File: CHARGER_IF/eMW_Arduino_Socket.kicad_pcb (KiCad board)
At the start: 2 copper layers, 18 x 33 mm, 2 parts, among them J4 CONN_02X10, U2 Arduino-Socket

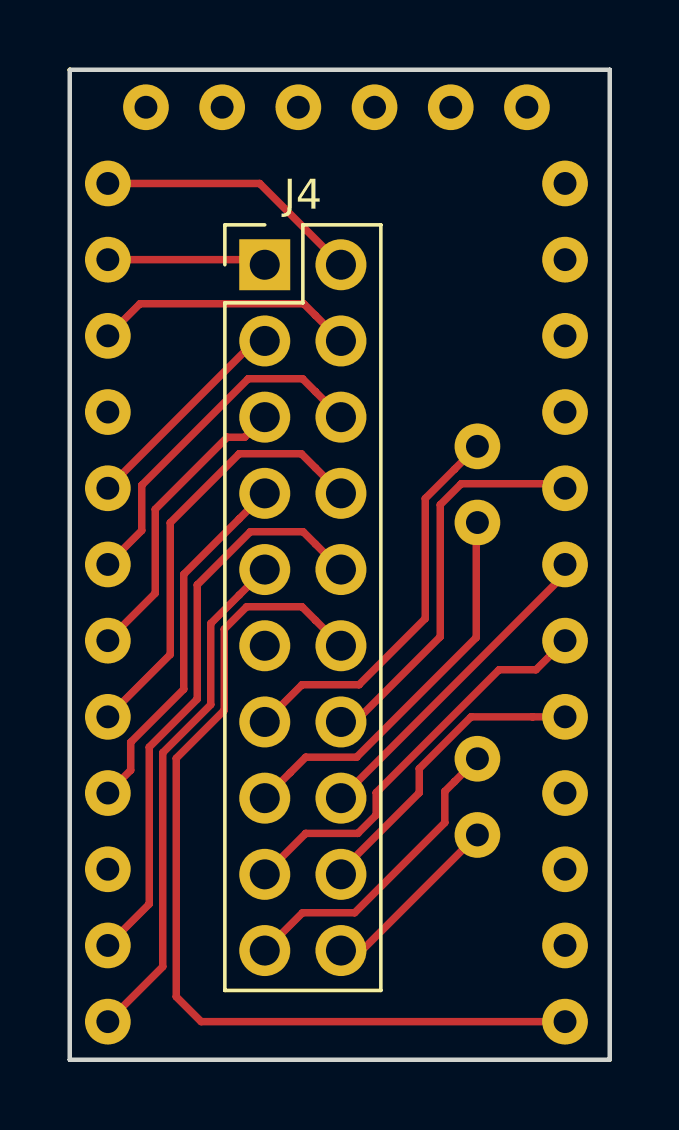
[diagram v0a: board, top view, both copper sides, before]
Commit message: updated to osh park design rules
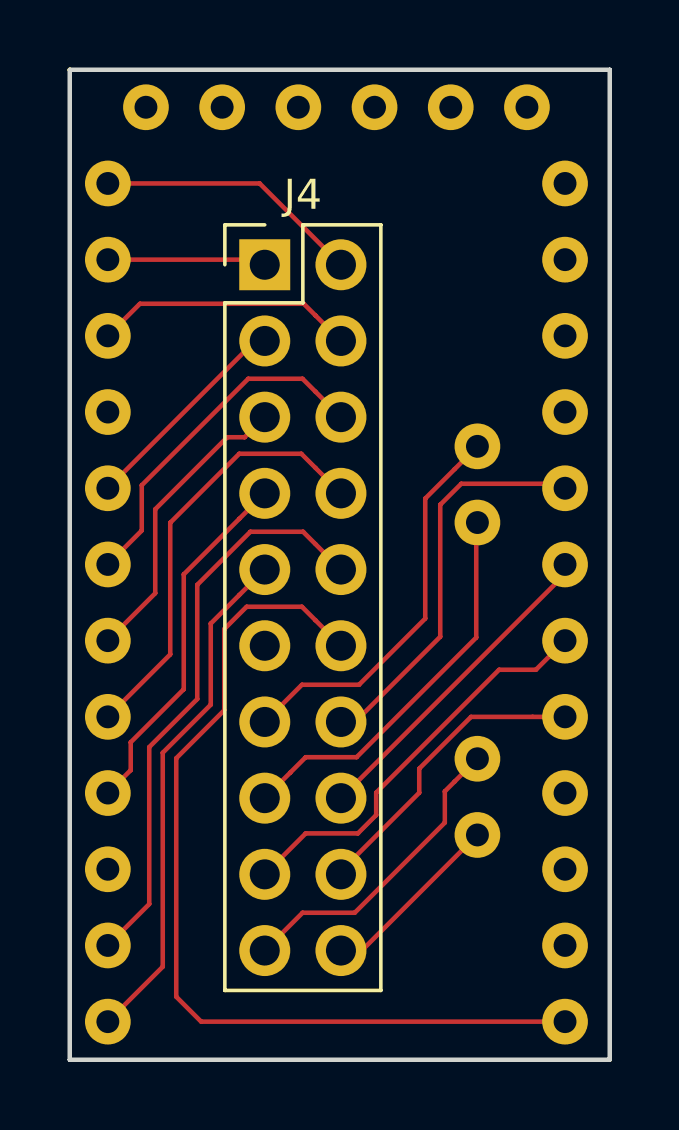
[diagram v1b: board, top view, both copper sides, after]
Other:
- net class Default: clearance 0.2 -> 0.1524; trace_width 0.25 -> 0.1524; via_dia 0.6 -> 0.6858; via_drill 0.4 -> 0.3302
- rule trace_clearance: 0.2 -> 0.1524
- rule trace_min: 0.2 -> 0.1524
- rule via_min_drill: 0.3 -> 0.3302
- rule via_min_size: 0.4 -> 0.6858

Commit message: Charger IF
needs double checking and pin labels on silkscreen
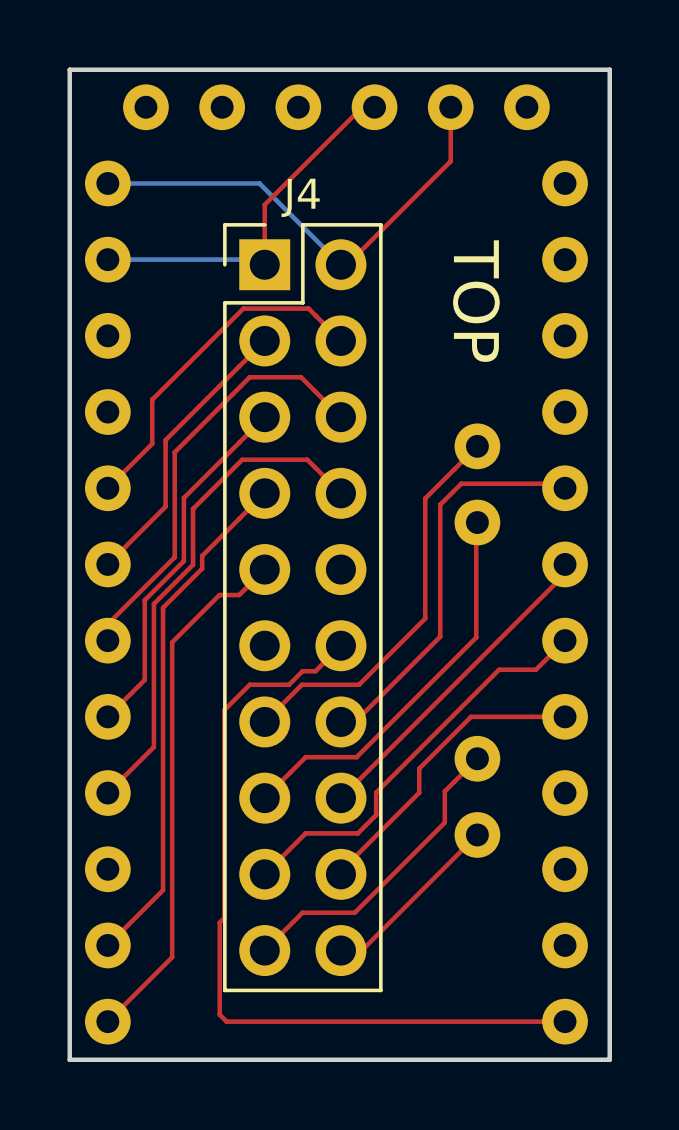
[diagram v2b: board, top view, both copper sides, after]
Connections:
- J4 pad 10: Net-(J4-Pad10) -> GND
- U2 pad 1: (no net) -> Net-(U2-Pad1)
- U2 pad 10: (no net) -> Net-(U2-Pad10)
- U2 pad 11: (no net) -> Net-(U2-Pad11)
- U2 pad 14: Net-(J4-Pad10) -> Net-(J4-Pad7)
- U2 pad 15: (no net) -> Net-(U2-Pad15)
- U2 pad 16: Net-(J4-Pad7) -> Net-(J4-Pad8)
- U2 pad 17: Net-(J4-Pad8) -> Net-(J4-Pad5)
- U2 pad 18: Net-(J4-Pad5) -> Net-(J4-Pad6)
- U2 pad 19: Net-(J4-Pad6) -> Net-(J4-Pad3)
- U2 pad 2: (no net) -> GND
- U2 pad 20: Net-(J4-Pad3) -> Net-(J4-Pad4)
- U2 pad 22: Net-(J4-Pad4) -> Net-(U2-Pad22)
- U2 pad 25: (no net) -> Net-(U2-Pad25)
- U2 pad 26: (no net) -> Net-(U2-Pad26)
- U2 pad 27: (no net) -> Net-(U2-Pad27)
- U2 pad 28: (no net) -> Net-(J4-Pad1)
- U2 pad 29: (no net) -> Net-(J4-Pad2)
- U2 pad 3: (no net) -> Net-(U2-Pad3)
- U2 pad 30: (no net) -> Net-(U2-Pad30)
- U2 pad 4: (no net) -> Net-(U2-Pad4)
- U2 pad 9: (no net) -> Net-(U2-Pad9)
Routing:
- net Net-(J4-Pad10): track 19.3 -> 0.00 mm
- net Net-(J4-Pad1): track 5.30 -> 12.5 mm
- net Net-(J4-Pad2): track 8.89 -> 15.8 mm
- net Net-(J4-Pad7): track 12.2 -> 17.2 mm
- net Net-(J4-Pad12): track 31.0 -> 26.6 mm
- net Net-(J4-Pad4): track 8.73 -> 11.6 mm
- net Net-(J4-Pad3): track 7.26 -> 9.94 mm
- net Net-(J4-Pad6): track 11.7 -> 14.3 mm
- net Net-(J4-Pad5): track 9.96 -> 12.2 mm
- net Net-(J4-Pad8): track 14.5 -> 16.7 mm
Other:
- board text added: "Bottom"
- board text added: "TOP"

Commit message: Final Charger IF
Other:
- board text added: "A0"
- board text added: "A1"
- board text added: "A2"
- board text added: "A3"
- board text added: "A4"
- board text added: "A5"
- board text added: "A6"
- board text added: "A7"
- board text added: "D11"
- board text added: "D2"
- board text added: "D3"
- board text added: "D4"
- board text added: "D5"
- board text added: "D6"
- board text added: "D7"
- board text added: "D8"
- board text added: "D9"
- board text added: "GND"
- board text added: "RX"
- board text added: "TX"
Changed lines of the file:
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@@
   (general
     (links 23)
-    (no_connects 2)
+    (no_connects 0)
     (area 134.174999 77.924999 152.325001 111.075001)
     (thickness 1.6)
-    (drawings 6)
+    (drawings 29)
     (tracks 105)
     (zones 0)
@@
       (net 30 "Net-(U2-Pad30)"))
   )
-  (gr_text Bottom (at 147.75 85 270) (layer B.SilkS)
+  (gr_text RX (at 144.25 81 180) (layer B.SilkS)
+    (effects (font (size 1 1) (thickness 0.1)) (justify mirror))
+  )
+  (gr_text RX (at 137.75 84.25 180) (layer B.SilkS)
+    (effects (font (size 1 1) (thickness 0.1)) (justify mirror))
+  )
+  (gr_text TX (at 146.75 81 180) (layer B.SilkS)
+    (effects (font (size 1 1) (thickness 0.1)) (justify mirror))
+  )
+  (gr_text TX (at 137.75 81.75 180) (layer B.SilkS)
+    (effects (font (size 1 1) (thickness 0.1)) (justify mirror))
+  )
+  (gr_text GND (at 148.5 84.25 180) (layer B.SilkS)
+    (effects (font (size 1 1) (thickness 0.1)) (justify mirror))
+  )
+  (gr_text GND (at 138 89.25 180) (layer B.SilkS)
+    (effects (font (size 1 1) (thickness 0.1)) (justify mirror))
+  )
+  (gr_text D11 (at 148.25 109.75 180) (layer B.SilkS)
+    (effects (font (size 1 1) (thickness 0.1)) (justify mirror))
+  )
+  (gr_text D9 (at 137.5 109.75 180) (layer B.SilkS)
+    (effects (font (size 1 1) (thickness 0.1)) (justify mirror))
+  )
+  (gr_text D8 (at 137.5 107 180) (layer B.SilkS)
+    (effects (font (size 1 1) (thickness 0.1)) (justify mirror))
+  )
+  (gr_text D7 (at 137.5 104.5 180) (layer B.SilkS)
+    (effects (font (size 1 1) (thickness 0.1)) (justify mirror))
+  )
+  (gr_text D6 (at 137.5 102 180) (layer B.SilkS)
+    (effects (font (size 1 1) (thickness 0.1)) (justify mirror))
+  )
+  (gr_text D5 (at 137.5 99.5 180) (layer B.SilkS)
+    (effects (font (size 1 1) (thickness 0.1)) (justify mirror))
+  )
+  (gr_text D4 (at 137.5 97 180) (layer B.SilkS)
+    (effects (font (size 1 1) (thickness 0.1)) (justify mirror))
+  )
+  (gr_text D3 (at 137.5 94.5 180) (layer B.SilkS)
+    (effects (font (size 1 1) (thickness 0.1)) (justify mirror))
+  )
+  (gr_text D2 (at 137.5 91.75 180) (layer B.SilkS)
+    (effects (font (size 1 1) (thickness 0.1)) (justify mirror))
+  )
+  (gr_text A7 (at 146 101 180) (layer B.SilkS)
+    (effects (font (size 1 1) (thickness 0.1)) (justify mirror))
+  )
+  (gr_text A6 (at 147.75 105.5 180) (layer B.SilkS)
+    (effects (font (size 1 1) (thickness 0.1)) (justify mirror))
+  )
+  (gr_text A5 (at 146 91.25 180) (layer B.SilkS)
+    (effects (font (size 1 1) (thickness 0.1)) (justify mirror))
+  )
+  (gr_text A4 (at 146 94.5 180) (layer B.SilkS)
+    (effects (font (size 1 1) (thickness 0.1)) (justify mirror))
+  )
+  (gr_text A3 (at 149.25 92 90) (layer B.SilkS)
+    (effects (font (size 1 1) (thickness 0.1)) (justify mirror))
+  )
+  (gr_text A2 (at 149 94.75 180) (layer B.SilkS)
+    (effects (font (size 1 1) (thickness 0.1)) (justify mirror))
+  )
+  (gr_text A1 (at 148.75 97 180) (layer B.SilkS)
+    (effects (font (size 1 1) (thickness 0.1)) (justify mirror))
+  )
+  (gr_text A0 (at 148.75 99.25 180) (layer B.SilkS)
+    (effects (font (size 1 1) (thickness 0.1)) (justify mirror))
+  )
+  (gr_text Bottom (at 146 86 270) (layer B.SilkS)
     (effects (font (size 1.5 1.5) (thickness 0.3)) (justify mirror))
   )

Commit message: Finals w/ pdf
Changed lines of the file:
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@@
     (links 23)
     (no_connects 0)
-    (area 134.174999 77.924999 152.325001 111.075001)
+    (area 132.0526 75.7826 152.325001 111.4024)
     (thickness 1.6)
     (drawings 29)
@@
     (visible_elements 7FFFFFFF)
     (pcbplotparams
-      (layerselection 0x00030_80000001)
+      (layerselection 0x010f0_80000001)
       (usegerberextensions false)
       (excludeedgelayer true)
@@
       (outputformat 1)
       (mirror false)
-      (drillshape 1)
+      (drillshape 0)
       (scaleselection 1)
-      (outputdirectory ""))
+      (outputdirectory "Arduino Socket Gerber/"))
   )
   (net 0 "")
@@
     (effects (font (size 1 1) (thickness 0.1)) (justify mirror))
   )
-  (gr_text Bottom (at 146 86 270) (layer B.SilkS)
+  (gr_text Bottom (at 146 86 270) (layer F.SilkS)
+    (effects (font (size 1.5 1.5) (thickness 0.3)))
+  )
+  (gr_text TOP (at 147.75 87.25 270) (layer B.SilkS)
     (effects (font (size 1.5 1.5) (thickness 0.3)) (justify mirror))
   )
-  (gr_text TOP (at 147.75 85.75 270) (layer F.SilkS)
-    (effects (font (size 1.5 1.5) (thickness 0.3)))
-  )
   (gr_line (start 152.25 78) (end 134.25 78) (angle 90) (layer Edge.Cuts) (width 0.15))

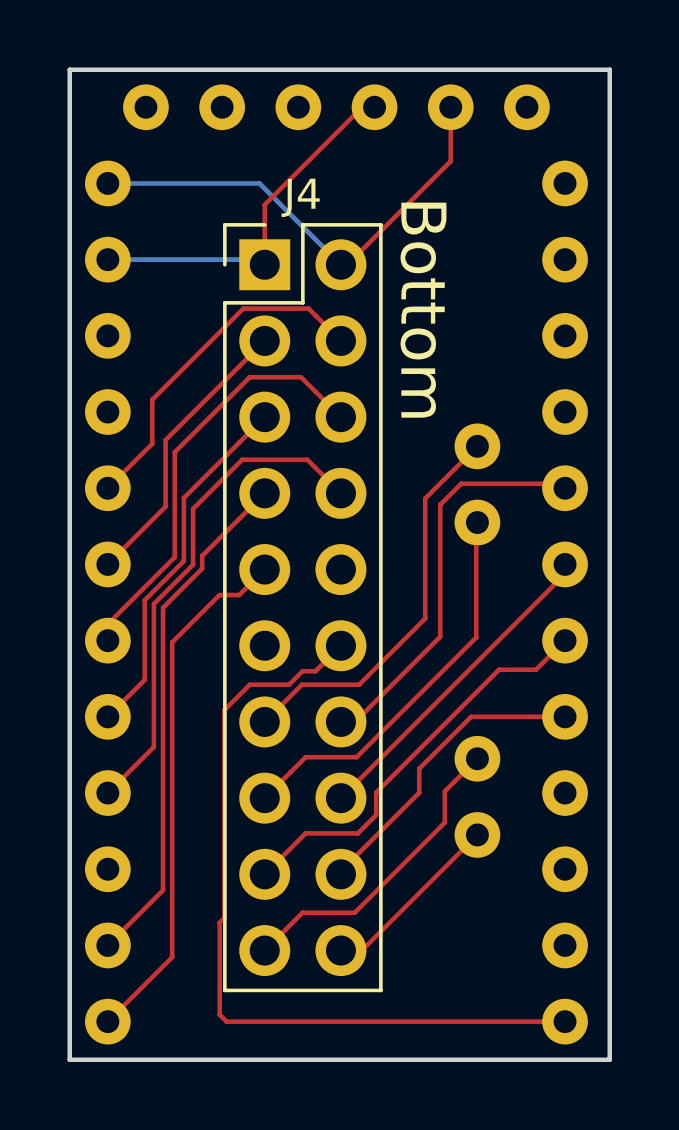
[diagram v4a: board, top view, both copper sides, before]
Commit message: fix arduino board header hole sizes
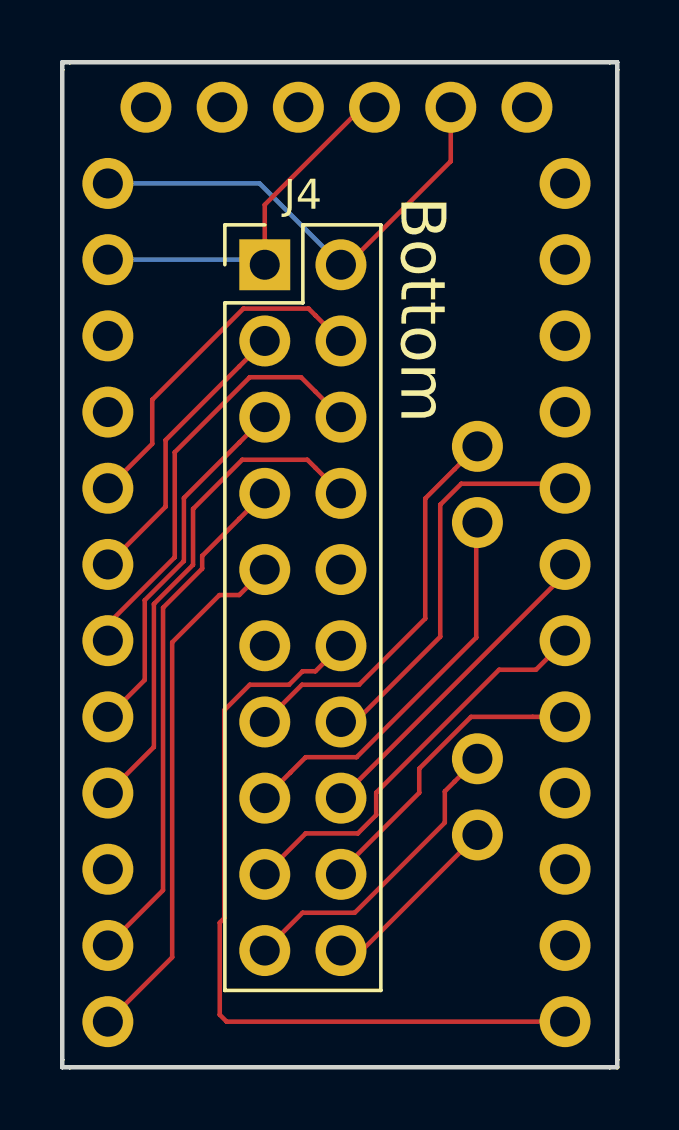
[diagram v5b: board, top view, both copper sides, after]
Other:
- board size 18 x 33 mm -> 18.5 x 33.5 mm
